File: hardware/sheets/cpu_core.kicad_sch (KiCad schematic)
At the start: 43 parts, among them U1 V20, U10 74HCT32, U11 74LVC125A, U12 74HC157, U13 74HCT04, U14 TCM809, U15 74LVC125A, U2 74LVC573A, U3 74LVC573A, U4 74LVC573A, U5 74LVC245A, U6 74HC138, U7 74HC00, U8 74LVC74A, U9 74LVC161

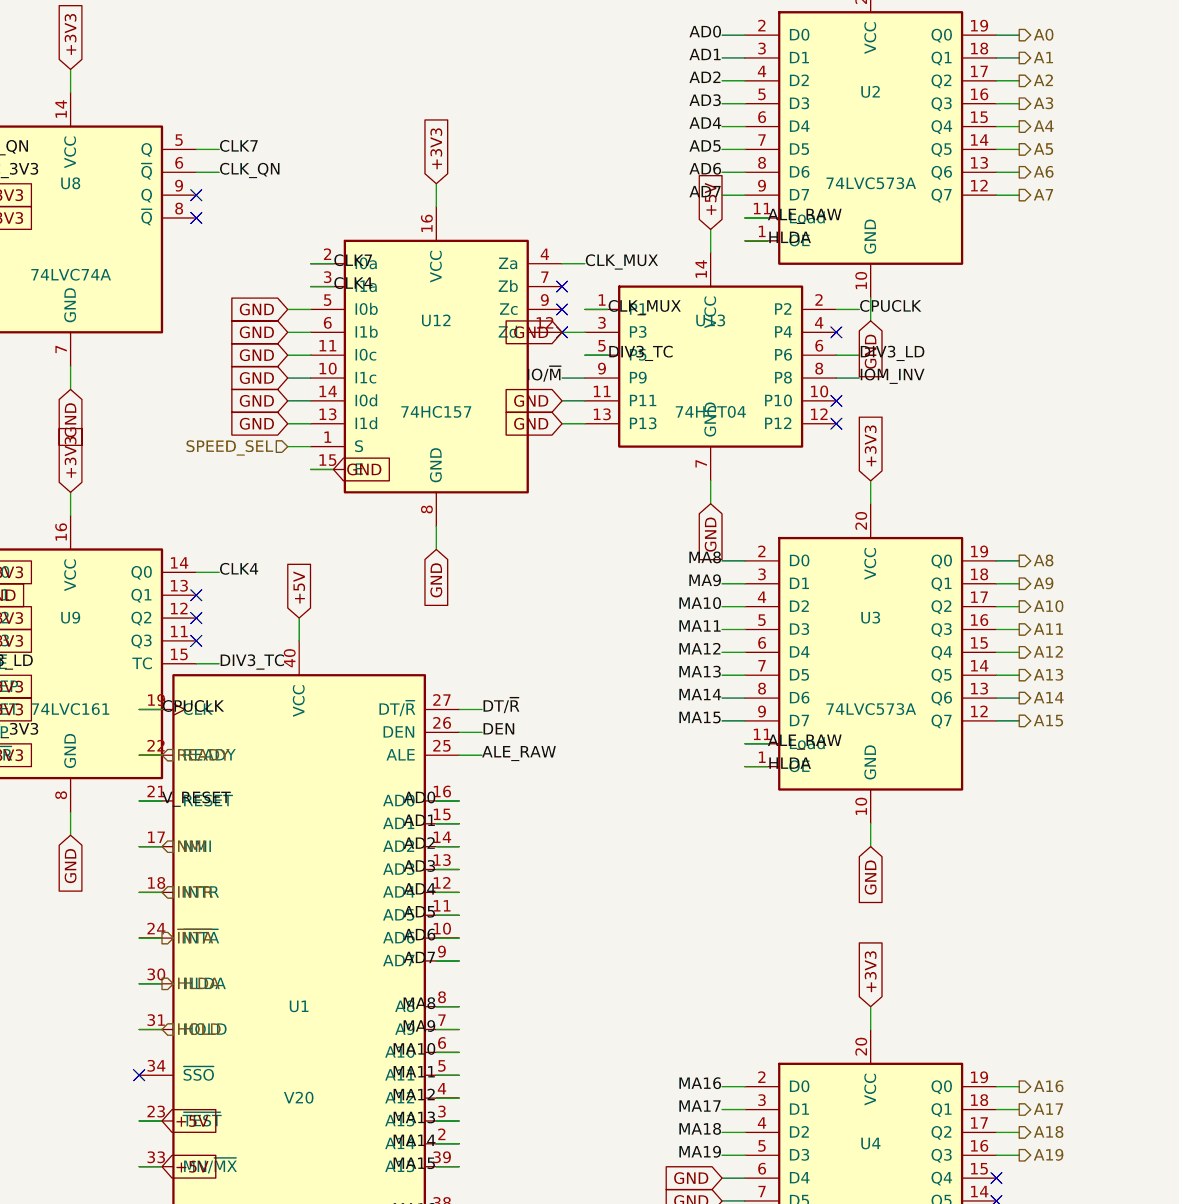
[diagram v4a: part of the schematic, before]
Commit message: 3.3V redesign: final-review fix wave (6 findings)
Reviewer-verified fixes, all at the generator level + regenerated outputs:

1. (Critical) bus_mcu U17 '04 @+3V3 had the V20's 5V HLDA on its input ->
   value-override to 74LVC04A (5V-tolerant input; parts.py binds C282341).
2. network R7 (AEN_CHIP park) +5V -> +3V3: it also feeds U5's '138 @+3V3;
   RTL8019AS AEN is 5V-TTL so 3.3V still reads high.
3. sidecar buf244(): tie unused '244 A inputs to GND, no_connect the Y
   outputs (U1105: 6 spare, U1108: 7) -- no floating always-enabled inputs.
4. MAX3241s (both com_port instances) +5V -> +3V3; charge-pump caps to the
   datasheet 3.0-3.6V column (all 0.1uF). Removes the 5V-R*OUT-into-3.3V-UART
   receiver path; com_port now has no +5V rail.
5. V20 READY/HOLD re-buffered through cpu_core U13's 3 spare '04 gates (zero
   package cost). READY = 2 gates (non-inverting), single-driver (no fold).
   HOLD = 1 inverting gate -> FIRMWARE MUST DRIVE HOLD ACTIVE-LOW at GPIO25
   (mxbus HOLD name intact). U13 nudged to clear a stub collision with U12.
6. Docs census + staleness: rewrote the 5V census to post-fix reality across
   CLAUDE.md, spec, design doc, README, irq-io-map (IRQ8 soft-PIC/undriven),
   parts.py header notes.

Build exit 0; check_parts 0 problems; all five sheets validate with zero
structural violations. Netlist evidence in questions-*.md.

Co-Authored-By: Claude Fable 5 <noreply@anthropic.com>
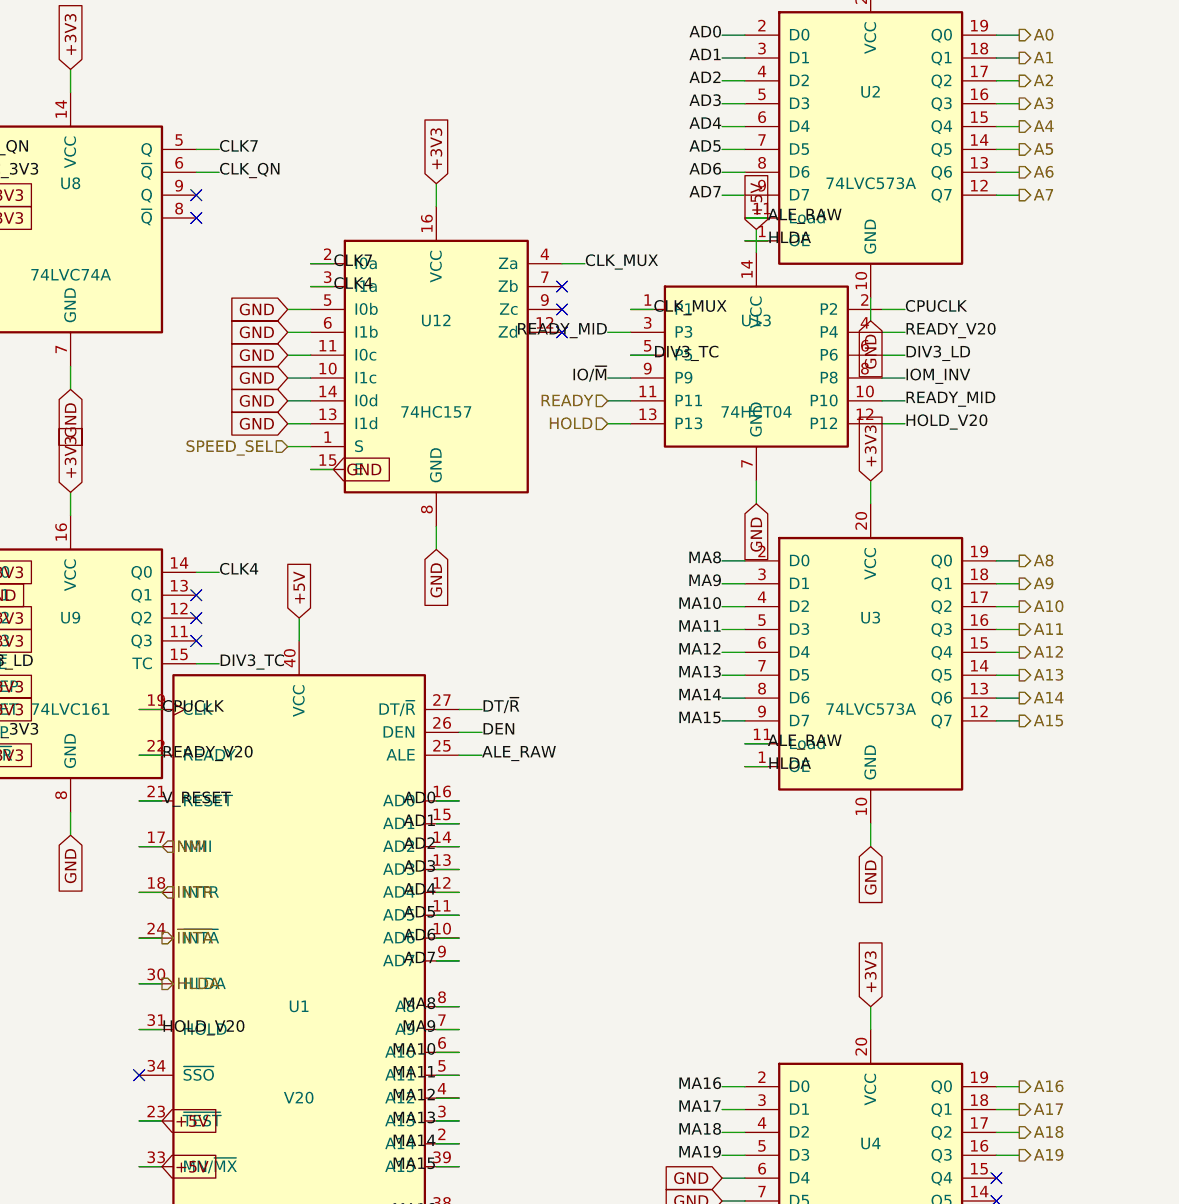
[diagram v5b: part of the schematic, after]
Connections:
- net GND: no longer U12.12 (Zd), U13.11 (P11), U13.13 (P13), U13.3 (P3)
- net HOLD: now also U13.13 (P13); no longer U1.31 (HOLD)
- net READY: now also U13.11 (P11); no longer U1.22 (READY)
- net READY_MID: now reaches U13.10 (P10)
- net READY_MID: now also U13.3 (P3)
- net HOLD_V20: now reaches U13.12 (P12)
- net HOLD_V20: now also U1.31 (HOLD)
- net READY_V20: now reaches U13.4 (P4)
- net READY_V20: now also U1.22 (READY)
- no-connect marks 24 -> 21
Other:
- moved on the sheet: U13
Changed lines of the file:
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@@
 		)
 	)
-	(hierarchical_label "HOLD"
-		(shape input)
+	(label "HOLD_V20"
 		(at 86.36 149.86 0)
 		(effects
@@
 		)
 	)
-	(hierarchical_label "READY"
-		(shape input)
+	(label "READY_V20"
 		(at 86.36 119.38 0)
 		(effects
@@
 	(wire
 		(pts
-			(xy 147.32 63.5)
-			(xy 147.32 60.96)
+			(xy 152.4 63.5)
+			(xy 152.4 60.96)
 		)
 		(stroke
@@
 	(global_label "+5V"
 		(shape input)
-		(at 147.32 60.96 90)
+		(at 152.4 60.96 90)
 		(effects
 			(font
@@
 	(wire
 		(pts
-			(xy 147.32 88.9)
-			(xy 147.32 91.44)
+			(xy 152.4 88.9)
+			(xy 152.4 91.44)
 		)
 		(stroke
@@
 	(global_label "GND"
 		(shape input)
-		(at 147.32 91.44 270)
+		(at 152.4 91.44 270)
 		(effects
 			(font
@@
 	(wire
 		(pts
-			(xy 133.35 69.85)
-			(xy 135.89 69.85)
+			(xy 138.43 69.85)
+			(xy 140.97 69.85)
 		)
 		(stroke
@@
 	)
 	(label "CLK_MUX"
-		(at 135.89 69.85 0)
+		(at 140.97 69.85 0)
 		(effects
 			(font
@@
 	(wire
 		(pts
-			(xy 161.29 69.85)
-			(xy 163.83 69.85)
+			(xy 166.37 69.85)
+			(xy 168.91 69.85)
 		)
 		(stroke
@@
 	)
 	(label "CPUCLK"
-		(at 163.83 69.85 0)
+		(at 168.91 69.85 0)
 		(effects
 			(font
@@
 	(wire
 		(pts
-			(xy 133.35 74.93)
-			(xy 135.89 74.93)
+			(xy 138.43 74.93)
+			(xy 140.97 74.93)
 		)
 		(stroke
@@
 	)
 	(label "DIV3_TC"
-		(at 135.89 74.93 0)
+		(at 140.97 74.93 0)
 		(effects
 			(font
@@
 	(wire
 		(pts
-			(xy 161.29 74.93)
-			(xy 163.83 74.93)
+			(xy 166.37 74.93)
+			(xy 168.91 74.93)
 		)
 		(stroke
@@
 	)
 	(label "DIV3_LD"
-		(at 163.83 74.93 0)
+		(at 168.91 74.93 0)
 		(effects
 			(font
@@
 	(wire
 		(pts
-			(xy 133.35 77.47)
-			(xy 130.81 77.47)
+			(xy 138.43 77.47)
+			(xy 135.89 77.47)
 		)
 		(stroke
@@
 	)
 	(label "IO/~{M}"
-		(at 130.81 77.47 180)
+		(at 135.89 77.47 180)
 		(effects
 			(font
@@
 	(wire
 		(pts
-			(xy 161.29 77.47)
-			(xy 163.83 77.47)
+			(xy 166.37 77.47)
+			(xy 168.91 77.47)
 		)
 		(stroke
@@
 	)
 	(label "IOM_INV"
-		(at 163.83 77.47 0)
+		(at 168.91 77.47 0)
 		(effects
 			(font
@@
 	(wire
 		(pts
-			(xy 133.35 80.01)
-			(xy 130.81 80.01)
+			(xy 138.43 80.01)
+			(xy 135.89 80.01)
 		)
 		(stroke
@@
 		)
 	)
-	(global_label "GND"
+	(hierarchical_label "READY"
 		(shape input)
-		(at 130.81 80.01 180)
+		(at 135.89 80.01 180)
 		(effects
 			(font
@@
 		)
 	)
-	(no_connect
-		(at 161.29 80.01)
+	(wire
+		(pts
+			(xy 166.37 80.01)
+			(xy 168.91 80.01)
+		)
+		(stroke
+			(width 0)
+			(type default)
+		)
+	)
+	(label "READY_MID"
+		(at 168.91 80.01 0)
+		(effects
+			(font
+				(size 1.27 1.27)
+			)
+		)
 	)
 	(wire
 		(pts
-			(xy 133.35 72.39)
-			(xy 130.81 72.39)
+			(xy 138.43 72.39)
+			(xy 135.89 72.39)
 		)
 		(stroke
@@
 		)
 	)
-	(global_label "GND"
-		(shape input)
-		(at 130.81 72.39 180)
+	(label "READY_MID"
+		(at 135.89 72.39 180)
 		(effects
 			(font
@@
 		)
 	)
-	(no_connect
-		(at 161.29 72.39)
+	(wire
+		(pts
+			(xy 166.37 72.39)
+			(xy 168.91 72.39)
+		)
+		(stroke
+			(width 0)
+			(type default)
+		)
+	)
+	(label "READY_V20"
+		(at 168.91 72.39 0)
+		(effects
+			(font
+				(size 1.27 1.27)
+			)
+		)
 	)
 	(wire
 		(pts
-			(xy 133.35 82.55)
-			(xy 130.81 82.55)
+			(xy 138.43 82.55)
+			(xy 135.89 82.55)
 		)
 		(stroke
@@
 		)
 	)
-	(global_label "GND"
+	(hierarchical_label "HOLD"
 		(shape input)
-		(at 130.81 82.55 180)
+		(at 135.89 82.55 180)
 		(effects
 			(font
@@
 		)
 	)
-	(no_connect
-		(at 161.29 82.55)
+	(wire
+		(pts
+			(xy 166.37 82.55)
+			(xy 168.91 82.55)
+		)
+		(stroke
+			(width 0)
+			(type default)
+		)
+	)
+	(label "HOLD_V20"
+		(at 168.91 82.55 0)
+		(effects
+			(font
+				(size 1.27 1.27)
+			)
+		)
 	)
 	(wire
@@
 	(symbol
 		(lib_id "mini-xt:74HCT04")
-		(at 147.32 76.2 0)
+		(at 152.4 76.2 0)
 		(unit 1)
 		(exclude_from_sim no)
@@
 		(fields_autoplaced yes)
 		(property "Reference" "U13"
-			(at 147.32 71.12 0)
+			(at 152.4 71.12 0)
 			(effects
 				(font
@@
 		)
 		(property "Value" "74HCT04"
-			(at 147.32 81.28 0)
+			(at 152.4 81.28 0)
 			(effects
 				(font
@@
 		)
 		(property "Footprint" "Package_SO:SOIC-14_3.9x8.7mm_P1.27mm"
-			(at 147.32 76.2 0)
+			(at 152.4 76.2 0)
 			(effects
 				(font
@@
 		)
 		(property "LCSC Part Num" "C672096"
-			(at 147.32 76.2 0)
+			(at 152.4 76.2 0)
 			(effects
 				(font

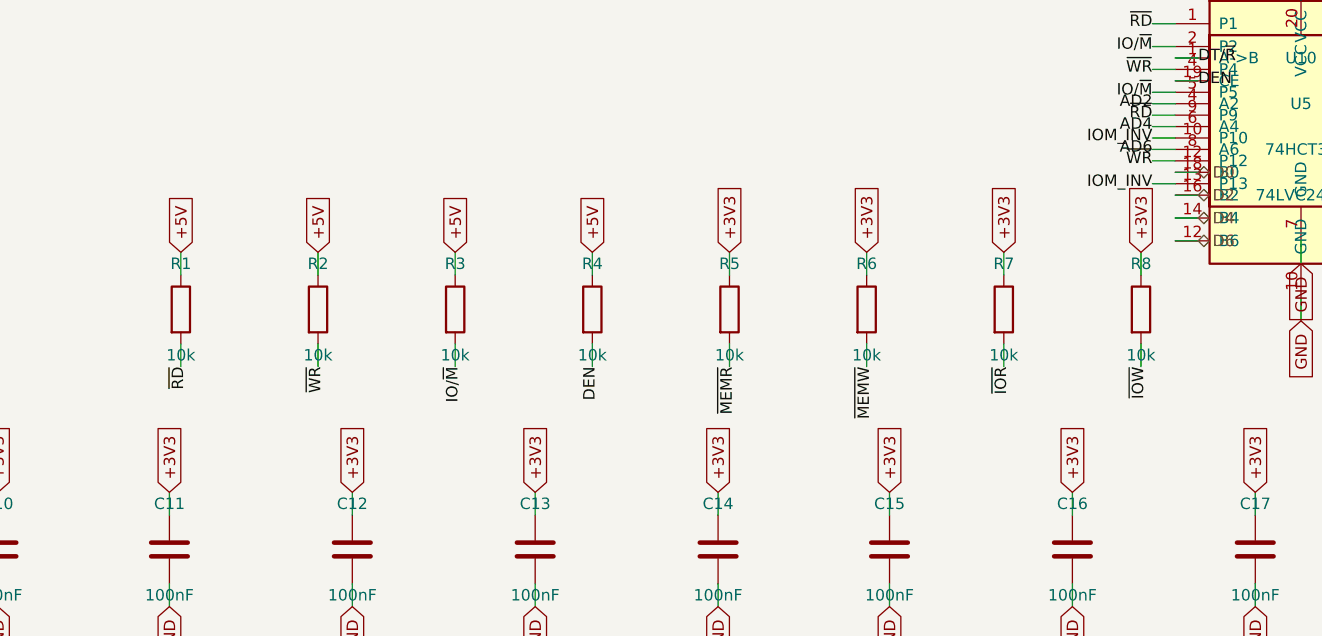
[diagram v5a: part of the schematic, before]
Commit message: Passives: basic-library audit + 4x resistor-array pull consolidation
Audit: every discrete R/C value was already JLC basic except the ferrite
beads -- swapped to basic Murata BLM18PG121SN1D (C14709, 120R@100MHz,
same family/role). The 100uF electrolytic and buck inductor stay
extended (zero fee-free parts exist in those subcategories). Pruned the
orphaned 5V-era 47nF/330nF MAX3241 cap entries.

Pull consolidation: 65 discrete 10k/4.7k rail pulls across 8 sheets
collapse into 18 basic 4-element isolated arrays (4D03WGJ0103T5E /
4D03WGJ0472T5E, element k = pins k/9-k; new mxbus.r_pack4 helper).
Isolated elements let packs mix rails; every net keeps its exact rail
and semantics (verified element-by-element in the netlist). RC/divider/
series/I2C resistors stay discrete. Board 452 -> 406 components; also
de-risks the sole basic 10k 0603 line (0 stock at audit). Audit
recorded in jlcpcb-sourcing.md.

Co-Authored-By: Claude Fable 5 <noreply@anthropic.com>
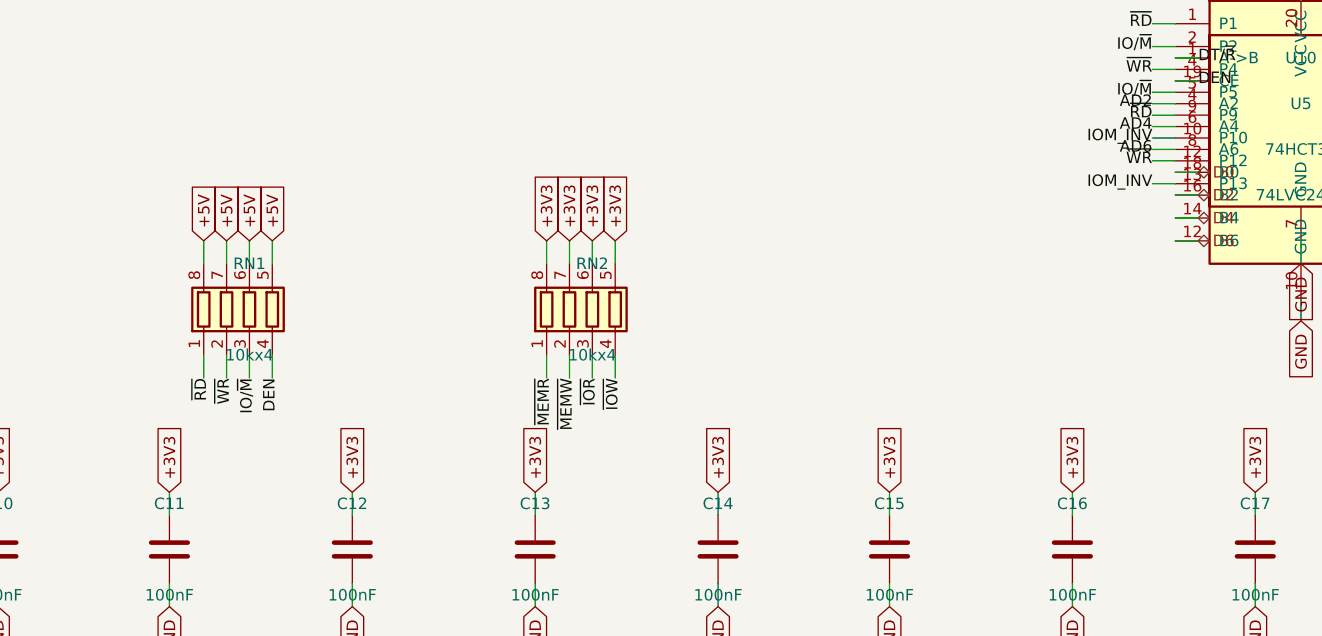
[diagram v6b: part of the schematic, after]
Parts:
- removed R2, R3, R4, R5, R6, R7, R8: 10k, Resistor_SMD:R_0603_1608Metric, symbol Device:R
- added RN2: 10kx4, Resistor_SMD:R_Array_Convex_4x0603, symbol Device:R_Pack04
- RN1: renamed from R1; value 10k -> 10kx4; footprint Resistor_SMD:R_0603_1608Metric -> Resistor_SMD:R_Array_Convex_4x0603; symbol Device:R -> Device:R_Pack04; LCSC Part Num C25804 -> C29718
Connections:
- net +3V3: now also RN2.5 (R4.2), RN2.6 (R3.2), RN2.7 (R2.2), RN2.8 (R1.2)
- net +5V: now also RN1.5 (R4.2), RN1.6 (R3.2), RN1.7 (R2.2), RN1.8 (R1.2); no longer RN1.1
- net DEN: now also RN1.4 (R4.1)
- net IO/~{M}: now also RN1.3 (R3.1)
- net ~{IOR}: now also RN2.3 (R3.1)
- net ~{IOW}: now also RN2.4 (R4.1)
- net ~{MEMR}: now also RN2.1 (R1.1)
- net ~{MEMW}: now also RN2.2 (R2.1)
- net ~{RD}: now also RN1.1 (R1.1); no longer RN1.2
- net ~{WR}: now also RN1.2 (R2.1)

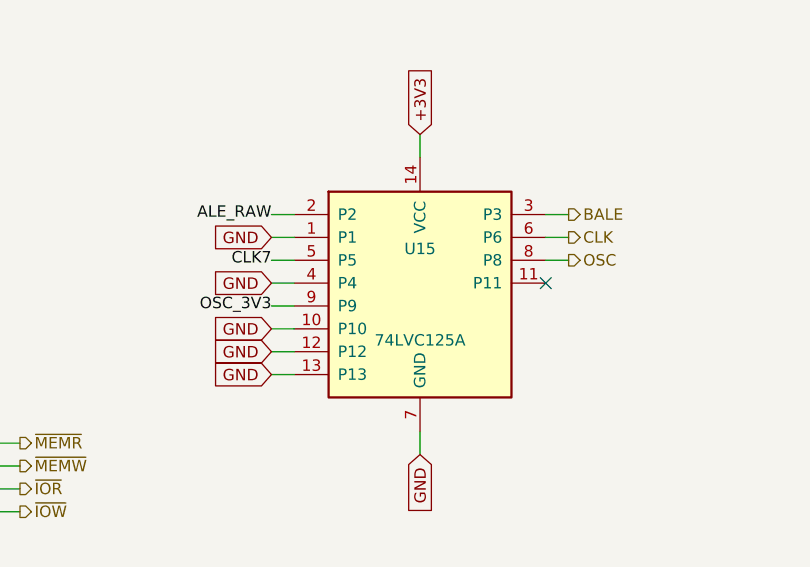
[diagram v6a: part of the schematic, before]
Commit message: Expansion port: 50-pin header, port DMA channel, dev cards deleted
Two waves of the 2026-07-14/15 expansion-port rework (the first was
uncommitted): the IRQ-scan collapse to one '165 + '32 OR rank with
ISA-card DMA removed outright, then the port redesign that brings one
DMA channel back:

- isa_conn: 60-pin (2x30, PicoGUS-standard layout) -> 50-pin (2x25,
  project-private pinout; 50-way IDC is far easier to source). OSC and
  ~REFRESH dropped to fit (no on-board consumer / no DRAM refresh; the
  planned ISA backplane board re-creates both for period cards).
- Port DMA: EXT_DRQ rides the sidecar inbound '244 + U12 '165 spare D6
  lane (zero GPIO); ~EXT_DACK = GPIO47 (freed by ~REFRESH) out through
  the strobe '244. Separate nets from the internal PicoGUS pair, so a
  port card never sees the on-board acknowledge.
- DRQ1/~DACK1 renamed DRQ/~DACK (ch2/3 long retired); DRQ2/3 +
  ~DACK2/3 removed from the mxbus contract.
- card_video + card_isatest deleted (sheets, hardware/cards/,
  build_cards()); superseded by the backplane plan. History has them.
- Connector parts: IDE header -> shrouded 2x20 IDC box (C9138, keypin
  20 NC'd); expansion port -> 90-degree 2x25 female socket (C21262364);
  addr_decode's five disable jumpers folded into ONE fixed 2x5 block
  JP1 (C492422), positions JP1.1-JP1.5 = COM1/COM2/LPT/IDE/VID.

ERC 0/0, check_parts 0 problems; docs/notes updated throughout.

Co-Authored-By: Claude Fable 5 <noreply@anthropic.com>
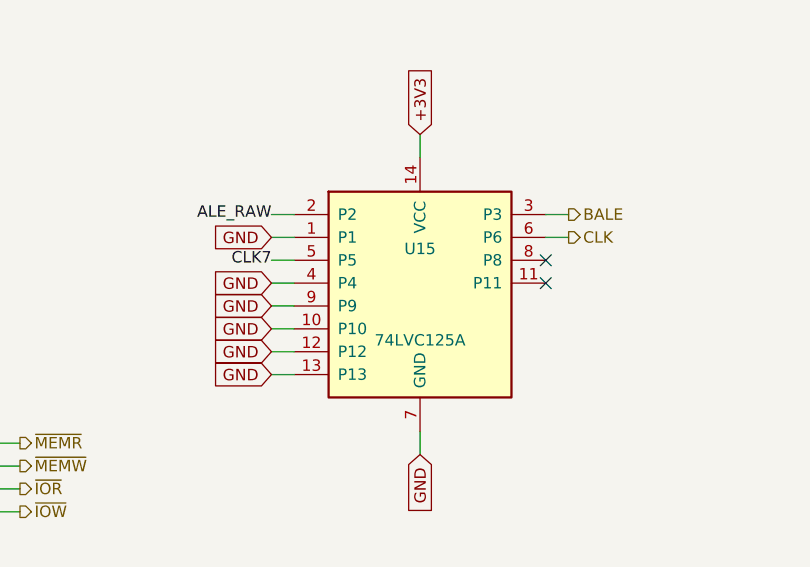
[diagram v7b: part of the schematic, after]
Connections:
- net GND: now also U15.9 (P9)
- net OSC_3V3: no longer U15.9 (P9)
- net OSC: no longer names the net of U15.8 (P8)
- no-connect marks 21 -> 22
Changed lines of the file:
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@@
 		)
 	)
-	(label "OSC_3V3"
+	(global_label "GND"
+		(shape input)
 		(at 250.19 196.85 180)
 		(effects
@@
 		)
 	)
-	(wire
-		(pts
-			(xy 280.67 191.77)
-			(xy 283.21 191.77)
-		)
-		(stroke
-			(width 0)
-			(type default)
-		)
-	)
-	(hierarchical_label "OSC"
-		(shape output)
-		(at 283.21 191.77 0)
-		(effects
-			(font
-				(size 1.27 1.27)
-			)
-		)
+	(no_connect
+		(at 280.67 191.77)
 	)
 	(wire
